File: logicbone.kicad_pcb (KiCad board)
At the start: 8 copper layers, 86.4 x 54.6 mm, 254 parts, among them IC1 ECP5UM-CABGA381, IC10 AT25SL128A, IC11 FAN5362UMP, IC12 74LVC1G07, IC13 TPS51206, IC14 KSZ9031RNXCA, IC15 TC7USB40MU, IC16 NCP349, IC17 NCP110AMX110, IC18 NCP110AMX110, IC19 NCP115AMX250, IC2 DDR3-TFBGA78, IC20 NCP115AMX250, IC3 DDR3-TFBGA78, IC4 MXL7704, IC5 PI6CG18401, IC6 74LVC1G02, IC7 FUSB302-QFN14, IC8 STM32FLxx-QFN48, IC9 ADC120, J1 NGFF-KEY-E, J2 GCT_USB4110_USBC, J3 ARJM11xx-502, J4 FTSH-105-DV-K, J5 Conn_02x05_Odd_Even, J6 Micro_SD_MEM2075, P8 BB_2x23, P9 BB_2x23, Q1 Q_PMOS_GSD, SW1 SW_SPST, SW2 SW_SPST, Y1 25MHz, Y2 32.768kHz

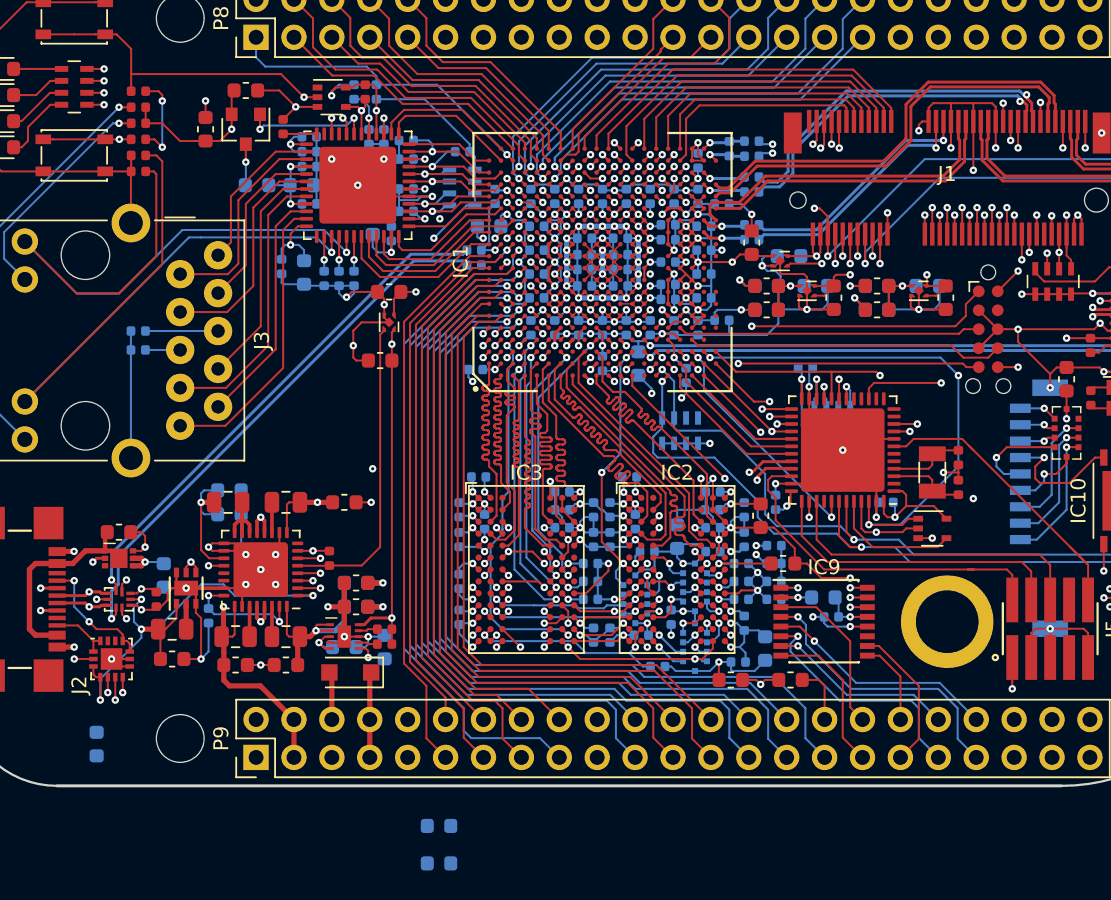
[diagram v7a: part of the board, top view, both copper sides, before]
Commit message: Add power fill zones for VCORE and DDR3 voltages.
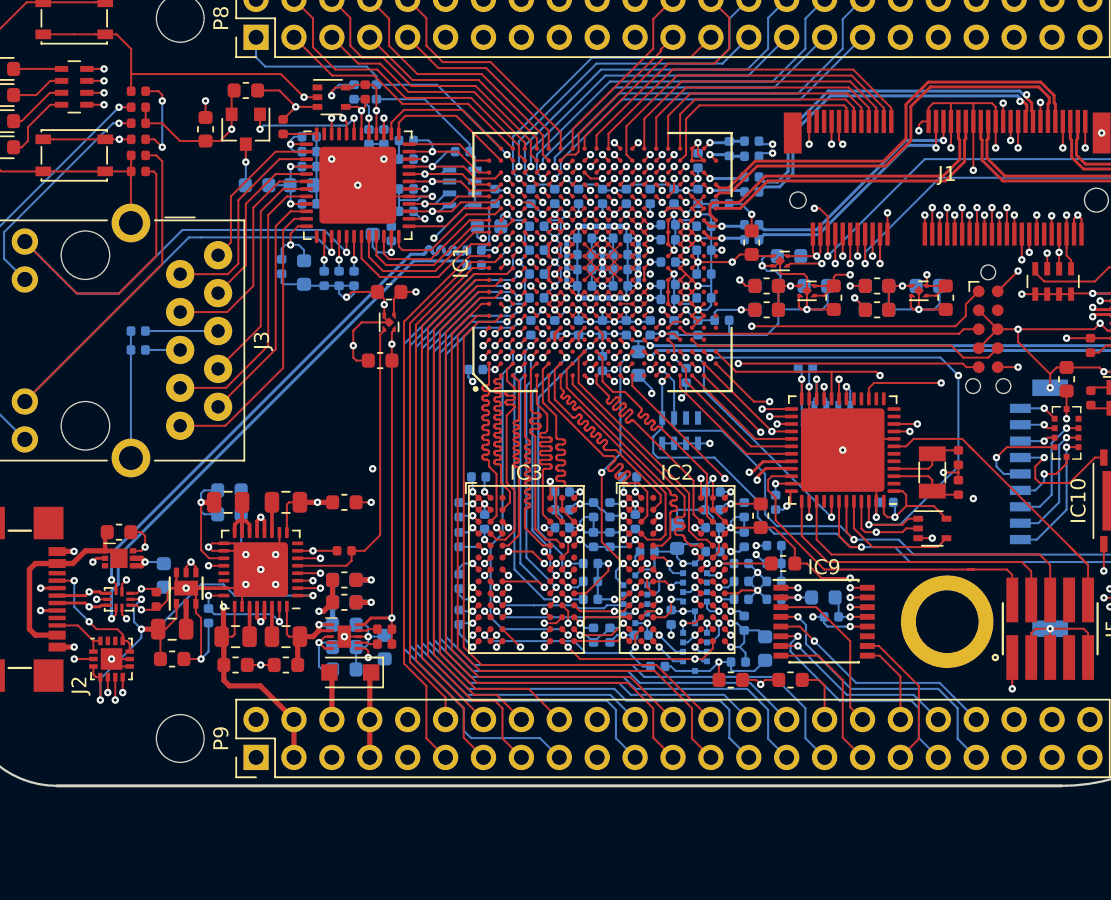
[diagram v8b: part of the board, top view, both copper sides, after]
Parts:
- removed C444: 10uF, Capacitor_SMD:C_0603_1608Metric
- moved C155 18.4 mm to (125.6, 89.2), turned to 0 degrees
- moved C445 12.3 mm to (125.6, 92.2)
- moved C416 2.08 mm to (135.0, 82.3)
- moved C464 2.08 mm to (133.3, 83.5)
- moved R18 1.12 mm to (125.6, 84.2), turned to 180 degrees
- moved C400 0.84 mm to (125.6, 87.7)
- moved FB9 0.84 mm to (125.6, 87.7)
- moved C410 0.81 mm to (125.6, 86.2)
- moved FB8 0.81 mm to (125.6, 86.2)
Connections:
- IC1 pad B3: /FPGA Memory/DDR3_A0 -> /FPGA Memory/DDR3_BA0
- IC1 pad B4: /FPGA Memory/DDR3_BA0 -> /FPGA Memory/DDR3_A0
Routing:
- net VDDR: track 85.3 -> 95.3 mm
- net /Supervisor/STM_USB-: track 60.4 -> 64.1 mm
- net VTT: track 64.6 -> 67.2 mm
- net /Ethernet/FPGA_USB+: track 34.9 -> 36.8 mm
- net GND: track 1315.7 -> 1317.7 mm, vias 146 -> 147
- net /FPGA SERDES/M2_USB_DM: track 1.88 -> 0.00 mm, vias 1 -> 0
- net /FPGA SERDES/M2_USB_DP: track 1.63 -> 0.00 mm, vias 1 -> 0
- net /DDR3 Power/VDDR_CORE: track 122.8 -> 124.2 mm
- net /FPGA Memory/DDR3_A0: track 32.3 -> 31.0 mm
- net /DDR3 Power/VDDR_IO: track 60.3 -> 61.7 mm
- net /FPGA Memory/DDR3_A2: track 37.3 -> 36.0 mm
- net /FPGA Memory/DDR3_VREF: track 105.5 -> 106.3 mm
- net /FPGA SERDES/PCIE_TX1+: track 23.0 -> 23.7 mm
- net /FPGA SERDES/PCIE_TX1-: track 23.5 -> 24.3 mm
- added copper zone on Pwr1.Cu, net /DDR3 Power/VDDR_CORE
- added copper zone on Pwr1.Cu, net /DDR3 Power/VDDR_IO
- added copper zone on Gnd2.Cu, net GND
- added copper zone on Pwr1.Cu, net VCORE
- added copper zone on Pwr1.Cu, net VDDR
- added copper zone on Pwr1.Cu, net VTT
